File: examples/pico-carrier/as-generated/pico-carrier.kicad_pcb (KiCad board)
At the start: 2 copper layers, 88 x 62 mm, 9 parts, among them J1 5V IN, J3 GP0-GP15, J4 GP16-GP28, PWR, U1 Pico

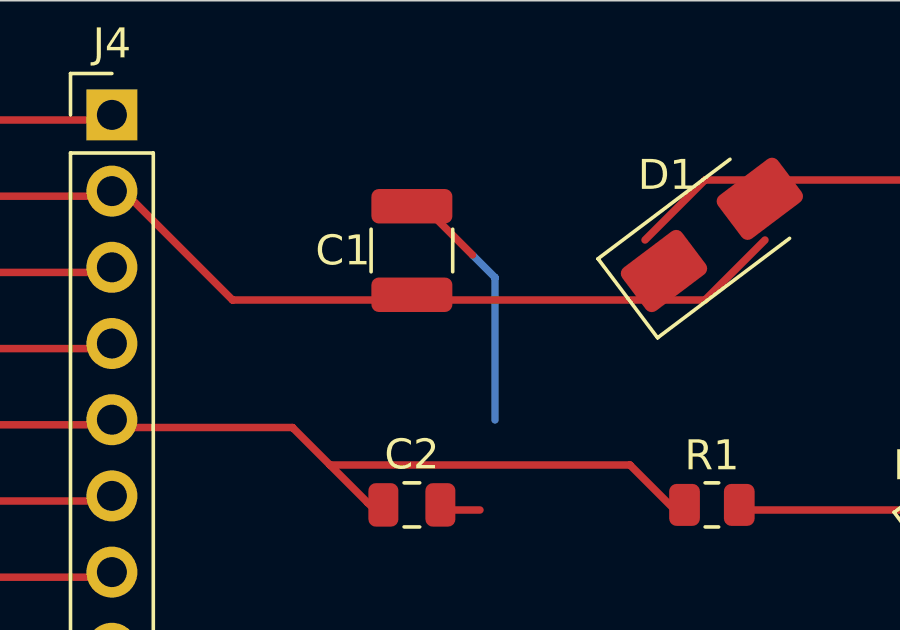
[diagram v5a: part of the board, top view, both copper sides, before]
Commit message: Give the vias room to stand beside the lands
Following the via-in-pad ban, the FPGA board stopped routing: five
attempts, five different nets, each one out of lanes in the corridor
between the FPGA's east escape fan and the codec's west one. Three
changes, in the order a layout would make them.

The via spacing was guesswork and is now the fab's. Hole to hole goes
from 1.2 mm to 0.9, which at the shipped 0.8/0.4 via leaves half a
millimetre of laminate between barrels - the ordinary minimum - and in a
1 mm-pitch escape comb is the difference between a lane and no lane.
What a via keeps off a land it may not sit in is its own radius plus a
solder-mask dam rather than the track clearance: the copper either side
may well be the same net, and what has to be true is that the mask can
part the barrel from the land.

Every decoupling capacitor now has its ground via placed against its own
pad rather than nine of them asking the search for one, and where the
via goes is chosen rather than fixed: `anchor_site` takes the nearest
position that clears everything already placed, fanning either side of
the direction facing off the part. A fixed offset walled off the
corridor its neighbour's supply needed - the via was legal, and it was
in the way.

And the seven parts sitting inside that corridor - four decoupling
capacitors, the two 1.2 V ones and the LED resistor - move four
millimetres south into the empty band below it. Twelve lanes leaving the
FPGA and ten arriving at the codec have eleven millimetres to cross in;
what a hand would do first is stop parking capacitors in the middle of
that, and it is the floorplan half of the debt this board's own README
has been carrying.

Co-Authored-By: Claude Fable 5 <noreply@anthropic.com>
Claude-Session: https://claude.ai/code/session_01DUj7Ltu92tWg159mCSacwY
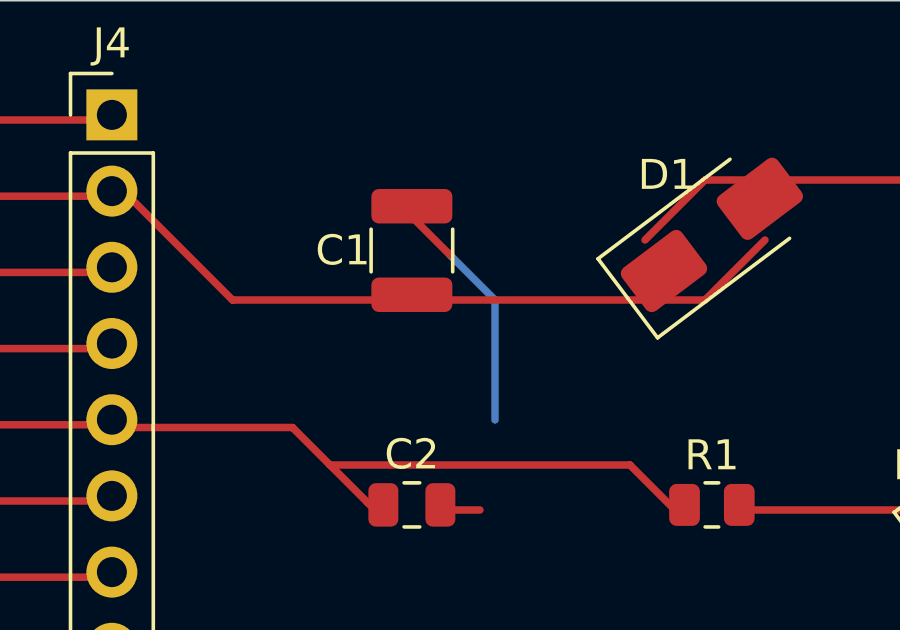
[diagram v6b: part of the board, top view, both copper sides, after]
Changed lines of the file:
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@@
 	(segment (start 135.69 94.48) (end 142.0 94.48) (width 0.25) (layer "F.Cu") (net 1))
 	(segment (start 135.69 107.18) (end 142.0 107.18) (width 0.25) (layer "F.Cu") (net 1))
-	(segment (start 152.0 67.045) (end 152.205 67.045) (width 0.25) (layer "F.Cu") (net 1))
-	(segment (start 152.205 67.045) (end 152.25 67.0) (width 0.25) (layer "F.Cu") (net 1))
-	(segment (start 152.25 67.0) (end 152.75 67.0) (width 0.25) (layer "F.Cu") (net 1))
-	(segment (start 152.75 67.0) (end 154.25 68.5) (width 0.25) (layer "F.Cu") (net 1))
-	(segment (start 154.25 68.5) (end 155.0 69.25) (width 0.25) (layer "B.Cu") (net 1))
-	(segment (start 155.0 69.25) (end 155.0 74.0) (width 0.25) (layer "B.Cu") (net 1))
+	(segment (start 152.0 67.045) (end 152.045 67.045) (width 0.25) (layer "F.Cu") (net 1))
+	(segment (start 152.045 67.045) (end 152.25 67.25) (width 0.25) (layer "F.Cu") (net 1))
+	(segment (start 152.25 67.25) (end 153.5 68.5) (width 0.25) (layer "F.Cu") (net 1))
+	(segment (start 153.5 68.5) (end 155.0 70.0) (width 0.25) (layer "B.Cu") (net 1))
+	(segment (start 155.0 70.0) (end 155.0 74.0) (width 0.25) (layer "B.Cu") (net 1))
 	(segment (start 152.95 77.0) (end 154.5 77.0) (width 0.25) (layer "F.Cu") (net 1))
 	(segment (start 170.9375 77.0) (end 171.0 77.0) (width 0.25) (layer "F.Cu") (net 1))

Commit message: Let KiCad fill the plane, and check the fill we actually ship
The reviewer saw copper pushing in between an 0603's pads and asked
whether DRC had been run at all. It had, and it was green, and both
things were true because the check and the drawing were looking at
different polygons.

The fill in the file was ours: a sweep of the pour outline with
everything of another net subtracted, written because a note here said
KiCad's own filler needs a display the container has not got. It does
not - `pcbnew`'s `ZONE_FILLER` runs headless in both images, and always
did by the time that note was written. Meanwhile `pcb drc` was passing
`--refill-zones`, so KiCad threw our polygons away and reported on a
fill of its own. Nobody was checking the one that ships, and it had
drifted: copper 0.075 mm from a foreign pad where the rule says 0.25,
and - measured just now with the refill turned off - two hundred pieces
of copper KiCad calls isolated.

So the zone is declared and left empty, and KiCad fills it: clearance,
minimum width and thermal relief all come from the board's own rules
instead of this file's idea of them. And `drc()` no longer refills a
board whose zones are already filled, because that fill is what goes to
the fab and what the plots draw. A board with an unfilled zone is still
refilled - otherwise every pad on that net reads as unconnected and the
report is noise - and `layout.unfilled_zone` says the file is
incomplete.

All five boards regenerate clean on both matrix versions against their
own committed fill: no errors, nothing unconnected, no isolated copper.
The plane no longer reaches between the passives' lands, and every
through-hole ground pad now has the four spokes of a thermal relief, so
an iron can bring the joint up without heating the whole plane.

The parser gains a pad's corner radius while measuring this, because a
roundrect land's bounding box is a quarter of a millimetre away from
where its copper is.

Co-Authored-By: Claude Fable 5 <noreply@anthr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
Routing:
- net GND: track 65.7 -> 60.4 mm
- net /LED_P: track 6.15 -> 11.5 mm

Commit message: Relieve the pads, fillet the joints, and give the board its screw holes
Three of the reviewer's manufacturing points, and they largely fall out
of the one before it - once KiCad fills the plane, the thermal relief it
was already asked for in the file actually appears.

**Thermal relief.** The zones said thermal all along; our own filler
ignored it and flooded every land solid. KiCad's does not, so every
through-hole ground pad now sits in a gap bridged by four spokes and an
iron can bring the joint up without heating a hundred square millimetres
of copper. `layout.solid_pad_connection` reports the setting when a
board turns it off: drilled pads only, because a surface pad reflows in
an oven that is heating the plane anyway and flooding it is often the
better thermal answer.

**Teardrops.** A track entering a land is a step change in width, and a
step change is where copper tears - the connector gets levered on and
off, the drill wanders, and the crack starts at the corner. `_teardrops`
replaces the first stretch of each run with a three-step taper into the
land, checked against its neighbours before it is kept, so a fillet
never eats the clearance a fine-pitch escape needs. It *replaces* rather
than overlays: laying the taper on top of the run drew the same copper
twice, and `route.acute_angle` reported all thirty of them, correctly.
`route.mixed_track_widths` learns what a fillet looks like so a properly
filleted board does not read as one nobody decided the width of.

**Mounting holes.** Four M3 holes near the corners, placed before the
router runs because they are obstacles, and slid along the edges or a
little inboard where a connector body has the corner - the motor board
and the op-amp take three, which is what those floorplans have room for.
Grounded on the motor driver, whose chassis is metal and part of the
shield, plain on the rest: bonding the enclosure to the reference is the
enclosure's decision, not the board's.

Two things that fell out of placing par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
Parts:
- added H1: M33, MountingHole:MountingHole_3.2mm_M3, F.Cu at (104.2, 63.8)
- added H2: M33, MountingHole:MountingHole_3.2mm_M3, F.Cu at (169.2, 63.8)
- added H3: M33, MountingHole:MountingHole_3.2mm_M3, F.Cu at (104.2, 117.8)
- added H4: M33, MountingHole:MountingHole_3.2mm_M3, F.Cu at (184.2, 117.8)
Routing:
- net /VSYS: track 30.6 -> 35.6 mm
